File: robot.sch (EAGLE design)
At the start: 2 parts

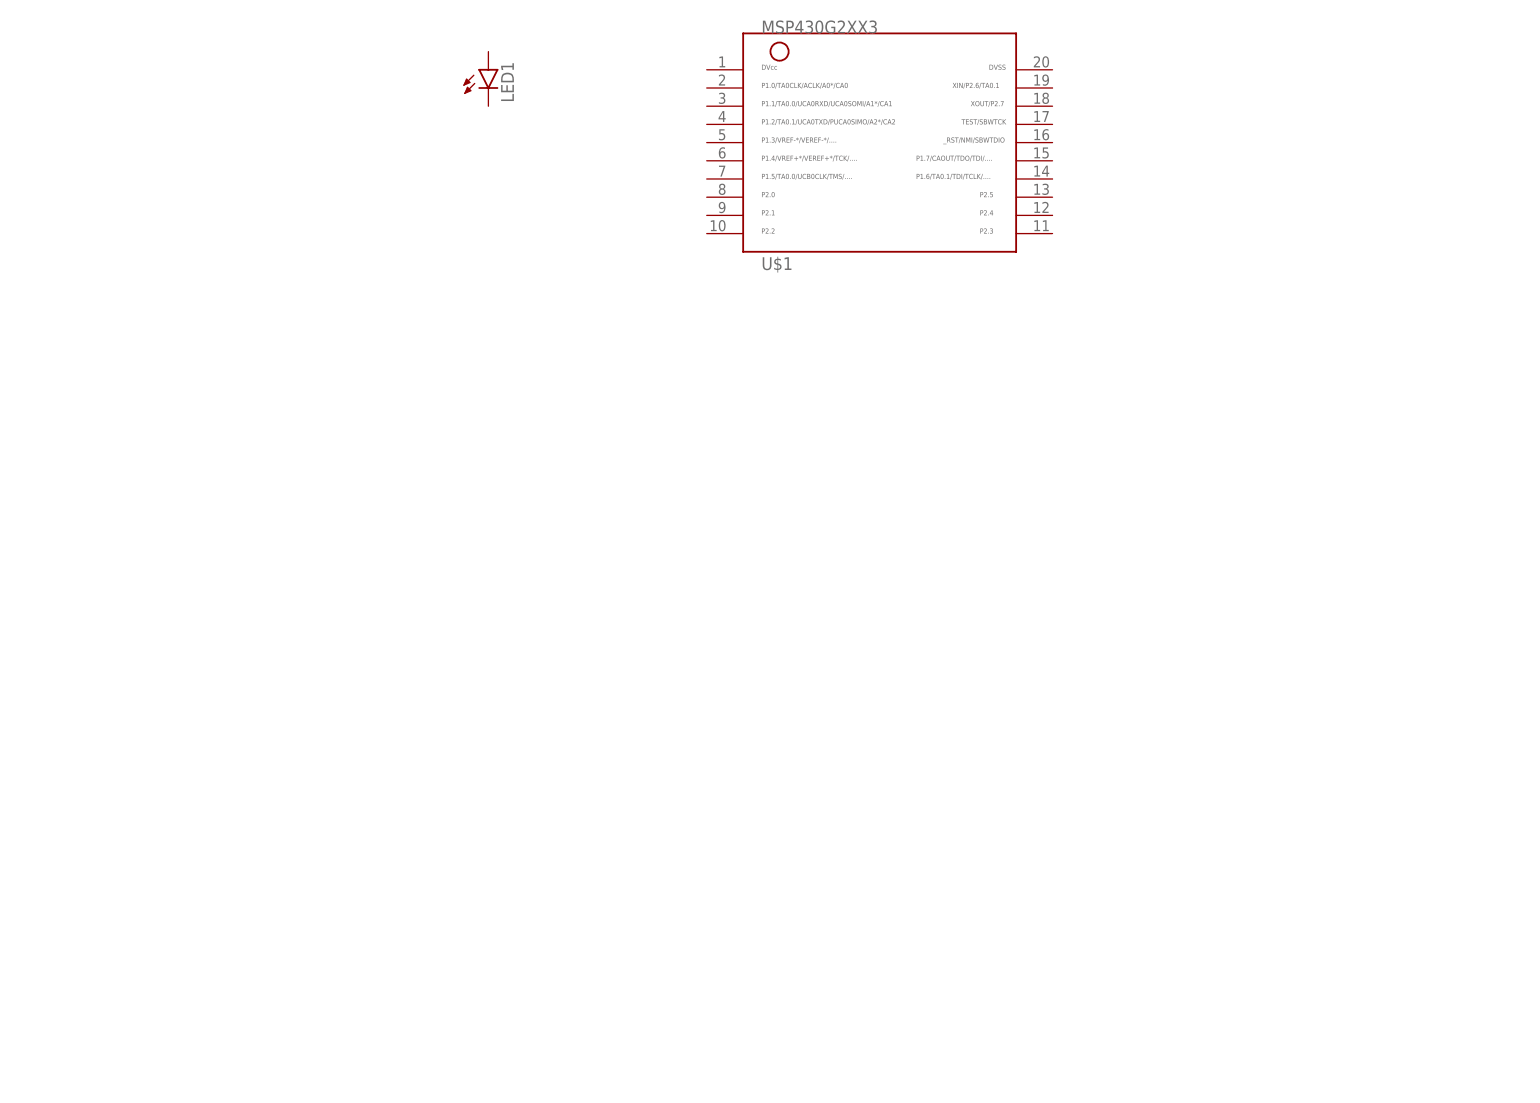
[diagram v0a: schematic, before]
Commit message: Added brushed motor controllers and voltage regulator.
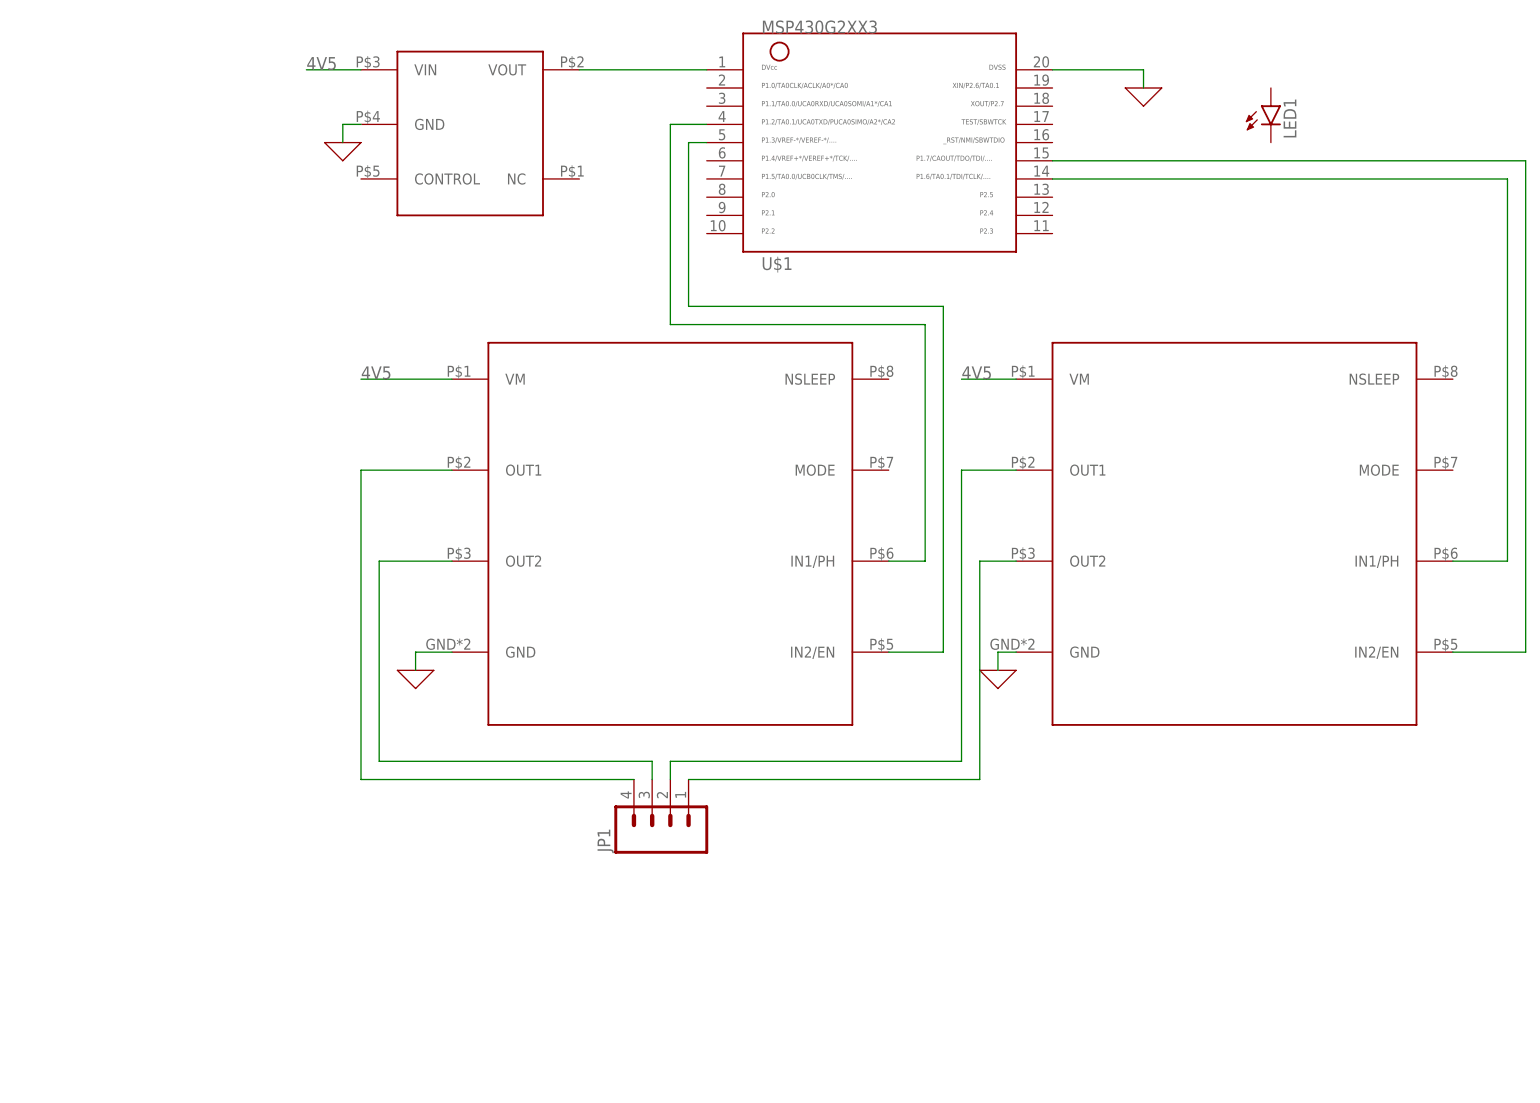
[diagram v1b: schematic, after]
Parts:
- added JP1: (no value), ELEC327:HEADER_1X04LOCK
- added U$2, U$3: DRV8220_H_BRIDGE, ELEC327:DRV8220_H_BRIDGE
- added U$4: TCR2EF3V3, ELEC327:TCR2EF3V3
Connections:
- new net 0: U$1.20, U$2.GND, U$3.GND, U$4.GND
- new net 4V5: U$2.VM, U$3.VM, U$4.VIN
- new net N$1: U$1.1, U$4.VOUT
- new net N$2: U$1.14, U$3.IN1/PH
- new net N$3: U$1.15, U$3.IN2/EN
- new net N$4: U$1.4, U$2.IN1/PH
- new net N$5: U$1.5, U$2.IN2/EN
- new net N$6: JP1.2, U$3.OUT1
- new net N$7: JP1.1, U$3.OUT2
- new net N$8: JP1.3, U$2.OUT2
- new net N$9: JP1.4, U$2.OUT1
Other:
- moved on the sheet: LED1
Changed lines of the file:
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@@
 <part name="U$1" library="ELEC327" deviceset="MSP430G2XX3" device="PDIP"/>
 <part name="LED1" library="led" library_urn="urn:adsk.eagle:library:259" deviceset="LED" device="5MM" package3d_urn="urn:adsk.eagle:package:15799/2"/>
+<part name="U$2" library="ELEC327" deviceset="DRV8220_H_BRIDGE" device=""/>
+<part name="U$3" library="ELEC327" deviceset="DRV8220_H_BRIDGE" device=""/>
+<part name="U$4" library="ELEC327" deviceset="TCR2EF3V3" device=""/>
+<part name="X_1" library="ngspice-simulation" library_urn="urn:adsk.eagle:library:527439" deviceset="GND" device=""/>
+<part name="X_2" library="ngspice-simulation" library_urn="urn:adsk.eagle:library:527439" deviceset="GND" device=""/>
+<part name="X_3" library="ngspice-simulation" library_urn="urn:adsk.eagle:library:527439" deviceset="GND" device=""/>
+<part name="X_4" library="ngspice-simulation" library_urn="urn:adsk.eagle:library:527439" deviceset="GND" device=""/>
+<part name="JP1" library="ELEC327" deviceset="HEADER_1X04" device="LOCK"/>
 </parts>
 <sheets>
@@
 <attribute name="NAME" x="53.34" y="43.18" size="1.778" layer="95"/>
 </instance>
-<instance part="LED1" gate="G$1" x="15.24" y="71.12" smashed="yes">
-<attribute name="NAME" x="18.796" y="66.548" size="1.778" layer="95" rot="R90"/>
-<attribute name="VALUE" x="20.955" y="66.548" size="1.778" layer="96" rot="R90"/>
+<instance part="LED1" gate="G$1" x="124.46" y="66.04" smashed="yes">
+<attribute name="NAME" x="128.016" y="61.468" size="1.778" layer="95" rot="R90"/>
+<attribute name="VALUE" x="130.175" y="61.468" size="1.778" layer="96" rot="R90"/>
+</instance>
+<instance part="U$2" gate="G$1" x="40.64" y="7.62" smashed="yes"/>
+<instance part="U$3" gate="G$1" x="119.38" y="7.62" smashed="yes"/>
+<instance part="U$4" gate="G$1" x="15.24" y="55.88" smashed="yes"/>
+<instance part="X_1" gate="G$1" x="106.68" y="68.58" smashed="yes"/>
+<instance part="X_2" gate="G$1" x="-5.08" y="60.96" smashed="yes"/>
+<instance part="X_3" gate="G$1" x="5.08" y="-12.7" smashed="yes"/>
+<instance part="X_4" gate="G$1" x="86.36" y="-12.7" smashed="yes"/>
+<instance part="JP1" gate="G$1" x="40.64" y="-33.02" smashed="yes" rot="R90">
+<attribute name="VALUE" x="48.26" y="-38.1" size="1.778" layer="96" rot="R90"/>
+<attribute name="NAME" x="32.258" y="-38.1" size="1.778" layer="95" rot="R90"/>
 </instance>
 </instances>
@@
 </busses>
 <nets>
+<net name="0" class="0">
+<segment>
+<pinref part="X_1" gate="G$1" pin="0"/>
+<wire x1="106.68" y1="68.58" x2="106.68" y2="71.12" width="0.1524" layer="91"/>
+<pinref part="U$1" gate="G$1" pin="20"/>
+<wire x1="106.68" y1="71.12" x2="93.98" y2="71.12" width="0.1524" layer="91"/>
+</segment>
+<segment>
+<pinref part="U$4" gate="G$1" pin="GND"/>
+<wire x1="-2.54" y1="63.5" x2="-5.08" y2="63.5" width="0.1524" layer="91"/>
+<pinref part="X_2" gate="G$1" pin="0"/>
+<wire x1="-5.08" y1="63.5" x2="-5.08" y2="60.96" width="0.1524" layer="91"/>
+</segment>
+<segment>
+<pinref part="U$2" gate="G$1" pin="GND"/>
+<wire x1="10.16" y1="-10.16" x2="5.08" y2="-10.16" width="0.1524" layer="91"/>
+<pinref part="X_3" gate="G$1" pin="0"/>
+<wire x1="5.08" y1="-10.16" x2="5.08" y2="-12.7" width="0.1524" layer="91"/>
+</segment>
+<segment>
+<pinref part="U$3" gate="G$1" pin="GND"/>
+<wire x1="88.9" y1="-10.16" x2="86.36" y2="-10.16" width="0.1524" layer="91"/>
+<pinref part="X_4" gate="G$1" pin="0"/>
+<wire x1="86.36" y1="-10.16" x2="86.36" y2="-12.7" width="0.1524" layer="91"/>
+</segment>
+</net>
+<net name="N$1" class="0">
+<segment>
+<pinref part="U$4" gate="G$1" pin="VOUT"/>
+<pinref part="U$1" gate="G$1" pin="1"/>
+<wire x1="27.94" y1="71.12" x2="45.72" y2="71.12" width="0.1524" layer="91"/>
+</segment>
+</net>
+<net name="N$2" class="0">
+<segment>
+<pinref part="U$1" gate="G$1" pin="14"/>
+<wire x1="93.98" y1="55.88" x2="157.48" y2="55.88" width="0.1524" layer="91"/>
+<pinref part="U$3" gate="G$1" pin="IN1/PH"/>
+<wire x1="157.48" y1="55.88" x2="157.48" y2="2.54" width="0.1524" layer="91"/>
+<wire x1="157.48" y1="2.54" x2="149.86" y2="2.54" width="0.1524" layer="91"/>
+</segment>
+</net>
+<net name="N$3" class="0">
+<segment>
+<pinref part="U$1" gate="G$1" pin="15"/>
+<wire x1="93.98" y1="58.42" x2="160.02" y2="58.42" width="0.1524" layer="91"/>
+<pinref part="U$3" gate="G$1" pin="IN2/EN"/>
+<wire x1="160.02" y1="58.42" x2="160.02" y2="-10.16" width="0.1524" layer="91"/>
+<wire x1="160.02" y1="-10.16" x2="149.86" y2="-10.16" width="0.1524" layer="91"/>
+</segment>
+</net>
+<net name="N$4" class="0">
+<segment>
+<pinref part="U$1" gate="G$1" pin="4"/>
+<wire x1="45.72" y1="63.5" x2="40.64" y2="63.5" width="0.1524" layer="91"/>
+<wire x1="40.64" y1="63.5" x2="40.64" y2="35.56" width="0.1524" layer="91"/>
+<wire x1="40.64" y1="35.56" x2="76.2" y2="35.56" width="0.1524" layer="91"/>
+<wire x1="76.2" y1="35.56" x2="76.2" y2="2.54" width="0.1524" layer="91"/>
+<pinref part="U$2" gate="G$1" pin="IN1/PH"/>
+<wire x1="76.2" y1="2.54" x2="71.12" y2="2.54" width="0.1524" layer="91"/>
+</segment>
+</net>
+<net name="N$5" class="0">
+<segment>
+<pinref part="U$2" gate="G$1" pin="IN2/EN"/>
+<wire x1="71.12" y1="-10.16" x2="78.74" y2="-10.16" width="0.1524" layer="91"/>
+<wire x1="78.74" y1="-10.16" x2="78.74" y2="38.1" width="0.1524" layer="91"/>
+<wire x1="78.74" y1="38.1" x2="43.18" y2="38.1" width="0.1524" layer="91"/>
+<pinref part="U$1" gate="G$1" pin="5"/>
+<wire x1="43.18" y1="38.1" x2="43.18" y2="60.96" width="0.1524" layer="91"/>
+<wire x1="43.18" y1="60.96" x2="45.72" y2="60.96" width="0.1524" layer="91"/>
+</segment>
+</net>
+<net name="N$6" class="0">
+<segment>
+<pinref part="U$3" gate="G$1" pin="OUT1"/>
+<wire x1="88.9" y1="15.24" x2="81.28" y2="15.24" width="0.1524" layer="91"/>
+<wire x1="81.28" y1="15.24" x2="81.28" y2="-25.4" width="0.1524" layer="91"/>
+<wire x1="81.28" y1="-25.4" x2="40.64" y2="-25.4" width="0.1524" layer="91"/>
+<pinref part="JP1" gate="G$1" pin="2"/>
+<wire x1="40.64" y1="-25.4" x2="40.64" y2="-27.94" width="0.1524" layer="91"/>
+</segment>
+</net>
+<net name="N$7" class="0">
+<segment>
+<pinref part="U$3" gate="G$1" pin="OUT2"/>
+<wire x1="88.9" y1="2.54" x2="83.82" y2="2.54" width="0.1524" layer="91"/>
+<wire x1="83.82" y1="2.54" x2="83.82" y2="-27.94" width="0.1524" layer="91"/>
+<pinref part="JP1" gate="G$1" pin="1"/>
+<wire x1="83.82" y1="-27.94" x2="43.18" y2="-27.94" width="0.1524" layer="91"/>
+</segment>
+</net>
+<net name="N$8" class="0">
+<segment>
+<pinref part="U$2" gate="G$1" pin="OUT2"/>
+<wire x1="10.16" y1="2.54" x2="0" y2="2.54" width="0.1524" layer="91"/>
+<wire x1="0" y1="2.54" x2="0" y2="-25.4" width="0.1524" layer="91"/>
+<wire x1="0" y1="-25.4" x2="38.1" y2="-25.4" width="0.1524" layer="91"/>
+<pinref part="JP1" gate="G$1" pin="3"/>
+<wire x1="38.1" y1="-25.4" x2="38.1" y2="-27.94" width="0.1524" layer="91"/>
+</segment>
+</net>
+<net name="N$9" class="0">
+<segment>
+<pinref part="JP1" gate="G$1" pin="4"/>
+<wire x1="35.56" y1="-27.94" x2="-2.54" y2="-27.94" width="0.1524" layer="91"/>
+<wire x1="-2.54" y1="-27.94" x2="-2.54" y2="15.24" width="0.1524" layer="91"/>
+<pinref part="U$2" gate="G$1" pin="OUT1"/>
+<wire x1="-2.54" y1="15.24" x2="10.16" y2="15.24" width="0.1524" layer="91"/>
+</segment>
+</net>
+<net name="4V5" class="0">
+<segment>
+<pinref part="U$4" gate="G$1" pin="VIN"/>
+<wire x1="-2.54" y1="71.12" x2="-10.16" y2="71.12" width="0.1524" layer="91"/>
+<label x="-10.16" y="71.12" size="1.778" layer="95"/>
+</segment>
+<segment>
+<pinref part="U$2" gate="G$1" pin="VM"/>
+<wire x1="10.16" y1="27.94" x2="-2.54" y2="27.94" width="0.1524" layer="91"/>
+<label x="-2.54" y="27.94" size="1.778" layer="95"/>
+</segment>
+<segment>
+<pinref part="U$3" gate="G$1" pin="VM"/>
+<wire x1="88.9" y1="27.94" x2="81.28" y2="27.94" width="0.1524" layer="91"/>
+<label x="81.28" y="27.94" size="1.778" layer="95"/>
+</segment>
+</net>
 </nets>
 </sheet>

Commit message: Only need one more footprint for the servo motor controller. Began connecting components in the schematic.
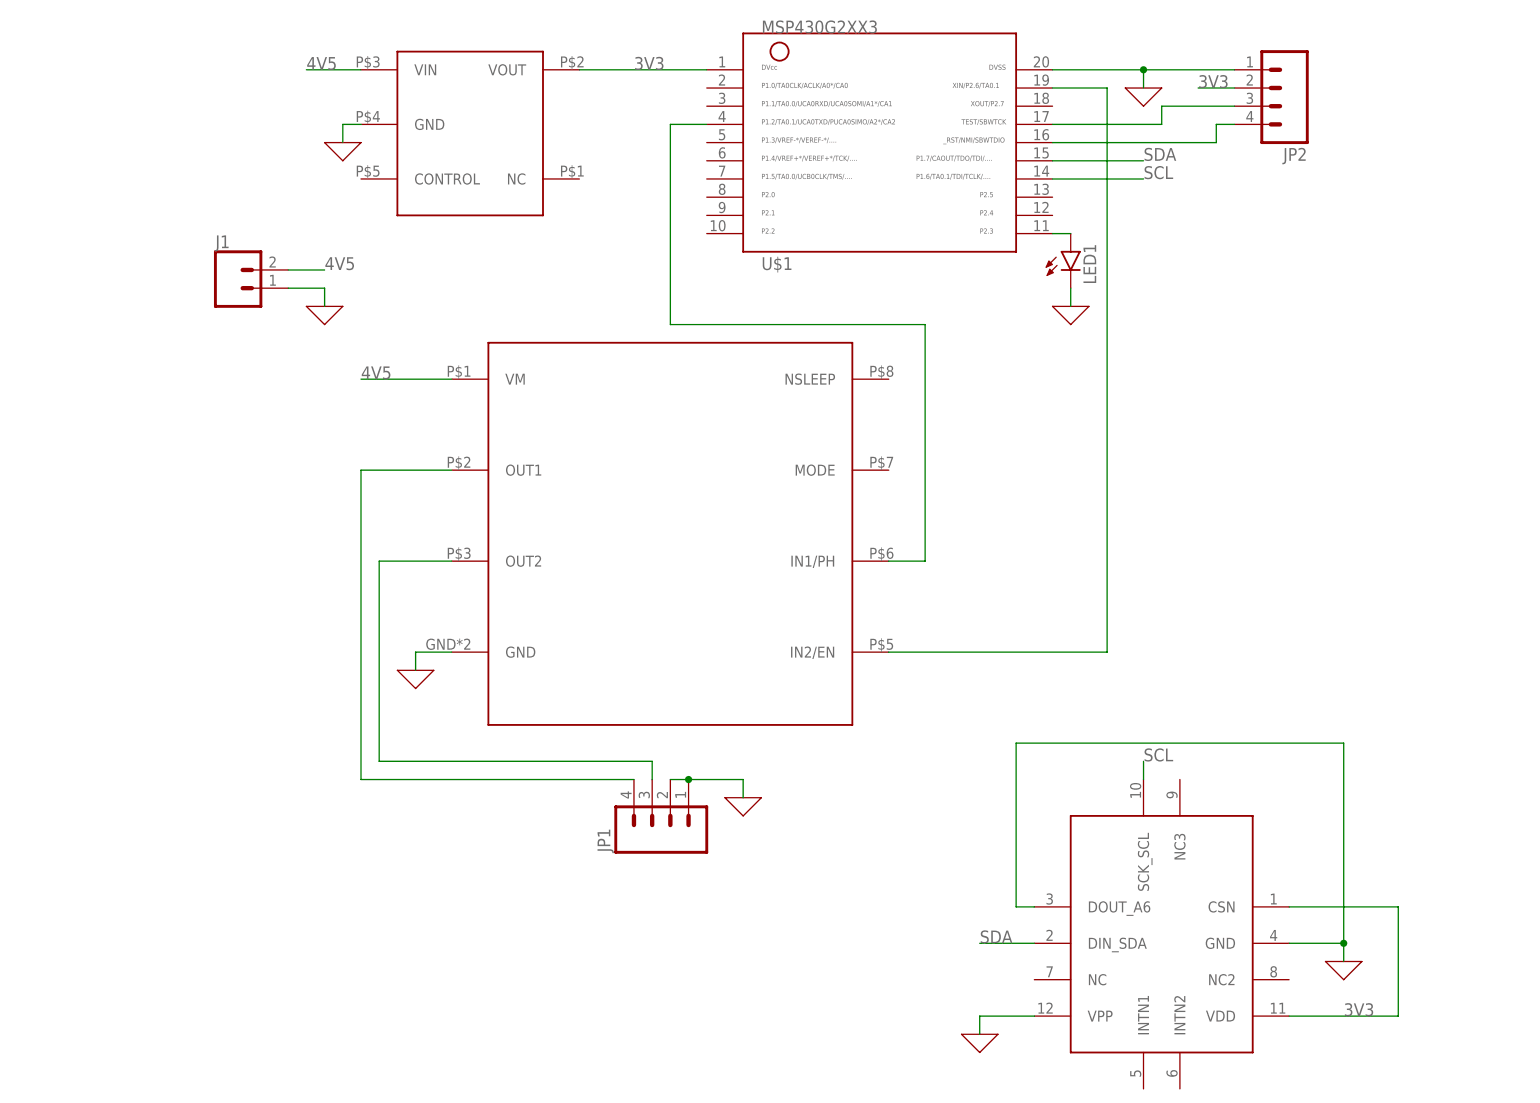
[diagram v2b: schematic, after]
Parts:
- removed U$3: DRV8220_H_BRIDGE, ELEC327:DRV8220_H_BRIDGE
- added J1: (no value), SparkFun-Connectors:CONN_02
- added JP2: (no value), ELEC327:HEADER_1X04LOCK
- added U$5: MC3419VFLGA-12, ELEC327:MC3419VFLGA-12
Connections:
- removed net N$2: U$1.14, U$3.IN1/PH
- removed net N$3: U$1.15, U$3.IN2/EN
- removed net N$6: JP1.2, U$3.OUT1
- removed net N$7: JP1.1, U$3.OUT2
- new net 3V3: JP2.2, U$1.1, U$4.VOUT, U$5.CSN, U$5.VDD
- new net N$10: JP2.3, U$1.17
- new net N$11: JP2.4, U$1.16
- new net SCL: U$1.14, U$5.SCK_SCL
- new net SDA: U$1.15, U$5.DIN_SDA
- net 0: now also J1.1, JP1.1, JP1.2, JP2.1, LED1.C, U$5.DOUT_A6, U$5.GND, U$5.VPP; no longer U$3.GND
- net 4V5: now also J1.2; no longer U$3.VM
- net N$1: now also LED1.A, U$1.11; no longer U$1.1, U$4.VOUT
- net N$5: now also U$1.19; no longer U$1.5
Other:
- moved on the sheet: LED1
